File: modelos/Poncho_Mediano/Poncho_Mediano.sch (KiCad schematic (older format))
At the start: 3 parts, among them P1 CONN_5, P2 CONN_4

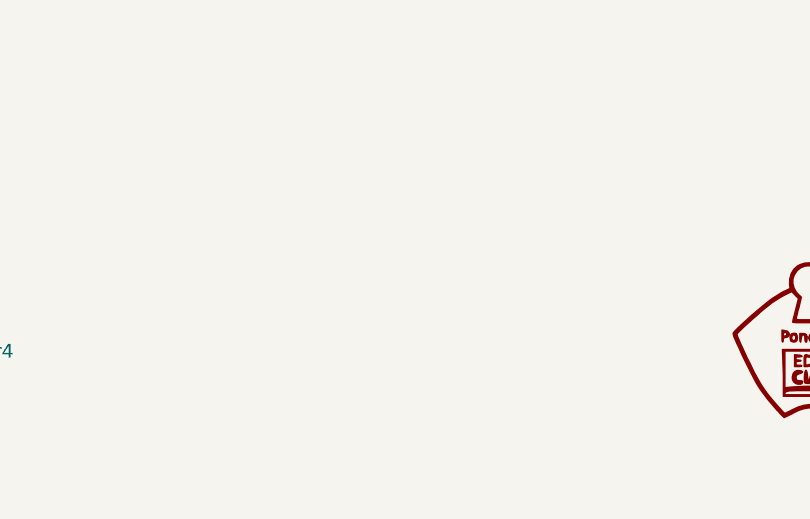
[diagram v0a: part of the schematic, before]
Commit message: * Agrego ruteo al poncho mediano. Muevo ícono de Template.
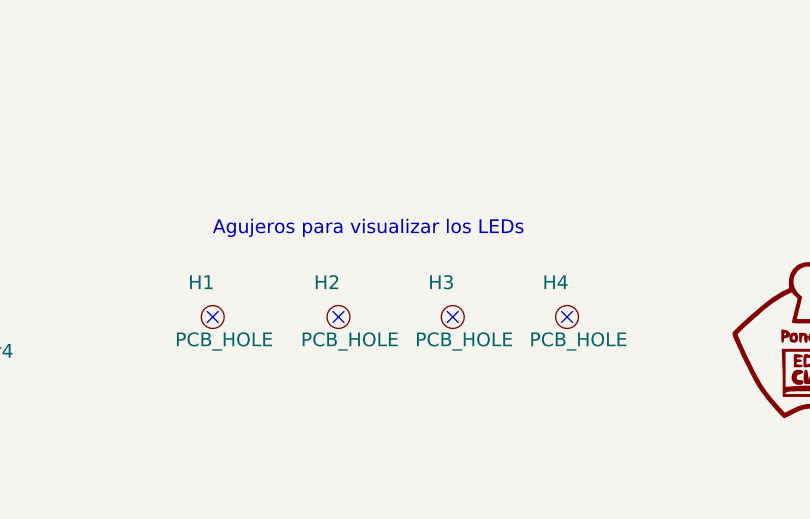
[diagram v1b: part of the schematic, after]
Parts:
- added H1, H2, H3, H4: PCB_HOLE, Poncho_Modelos:Led_Hole, symbol PCB_HOLE
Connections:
- no-connect marks 24 -> 28
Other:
- note added: "Agujeros para visualizar los LEDs"
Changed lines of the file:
@@
 Wire Wire Line
 	4850 6300 5400 6300
+$Comp
+L PCB_HOLE H1
+U 1 1 56145856
+P 7550 5900
+F 0 "H1" H 7500 6050 60  0000 C CNN
+F 1 "PCB_HOLE" H 7600 5800 60  0000 C CNN
+F 2 "Poncho_Modelos:Led_Hole" H 7400 5950 60  0001 C CNN
+F 3 "PCB HOLE" H 7500 6050 60  0001 C CNN
+	1    7550 5900
+	1    0    0    -1
+$EndComp
+$Comp
+L PCB_HOLE H2
+U 1 1 561458ED
+P 8100 5900
+F 0 "H2" H 8050 6050 60  0000 C CNN
+F 1 "PCB_HOLE" H 8150 5800 60  0000 C CNN
+F 2 "Poncho_Modelos:Led_Hole" H 7950 5950 60  0001 C CNN
+F 3 "PCB HOLE" H 8050 6050 60  0001 C CNN
+	1    8100 5900
+	1    0    0    -1
+$EndComp
+$Comp
+L PCB_HOLE H3
+U 1 1 56145920
+P 8600 5900
+F 0 "H3" H 8550 6050 60  0000 C CNN
+F 1 "PCB_HOLE" H 8650 5800 60  0000 C CNN
+F 2 "Poncho_Modelos:Led_Hole" H 8450 5950 60  0001 C CNN
+F 3 "PCB HOLE" H 8550 6050 60  0001 C CNN
+	1    8600 5900
+	1    0    0    -1
+$EndComp
+$Comp
+L PCB_HOLE H4
+U 1 1 56145951
+P 9100 5900
+F 0 "H4" H 9050 6050 60  0000 C CNN
+F 1 "PCB_HOLE" H 9150 5800 60  0000 C CNN
+F 2 "Poncho_Modelos:Led_Hole" H 8950 5950 60  0001 C CNN
+F 3 "PCB HOLE" H 9050 6050 60  0001 C CNN
+	1    9100 5900
+	1    0    0    -1
+$EndComp
+Text Notes 7550 5550 0    60   ~ 0
+Agujeros para visualizar los LEDs
+NoConn ~ 7550 5900
+NoConn ~ 8100 5900
+NoConn ~ 8600 5900
+NoConn ~ 9100 5900
 $EndSCHEMATC
